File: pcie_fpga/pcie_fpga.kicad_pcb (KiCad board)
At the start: 4 copper layers, 167.7 x 68.9 mm, 26 parts, among them J1 PMOD_Host_Conn_02x06, J2 PCIexpress_x8, J3 PMOD_Host_Conn_02x06, J4 PMOD_Host_Conn_02x06, J5 87832-1420, U2 XCAU10P-1FFVB676I, X1 ECS-2520MVQ-1000-BN-TR

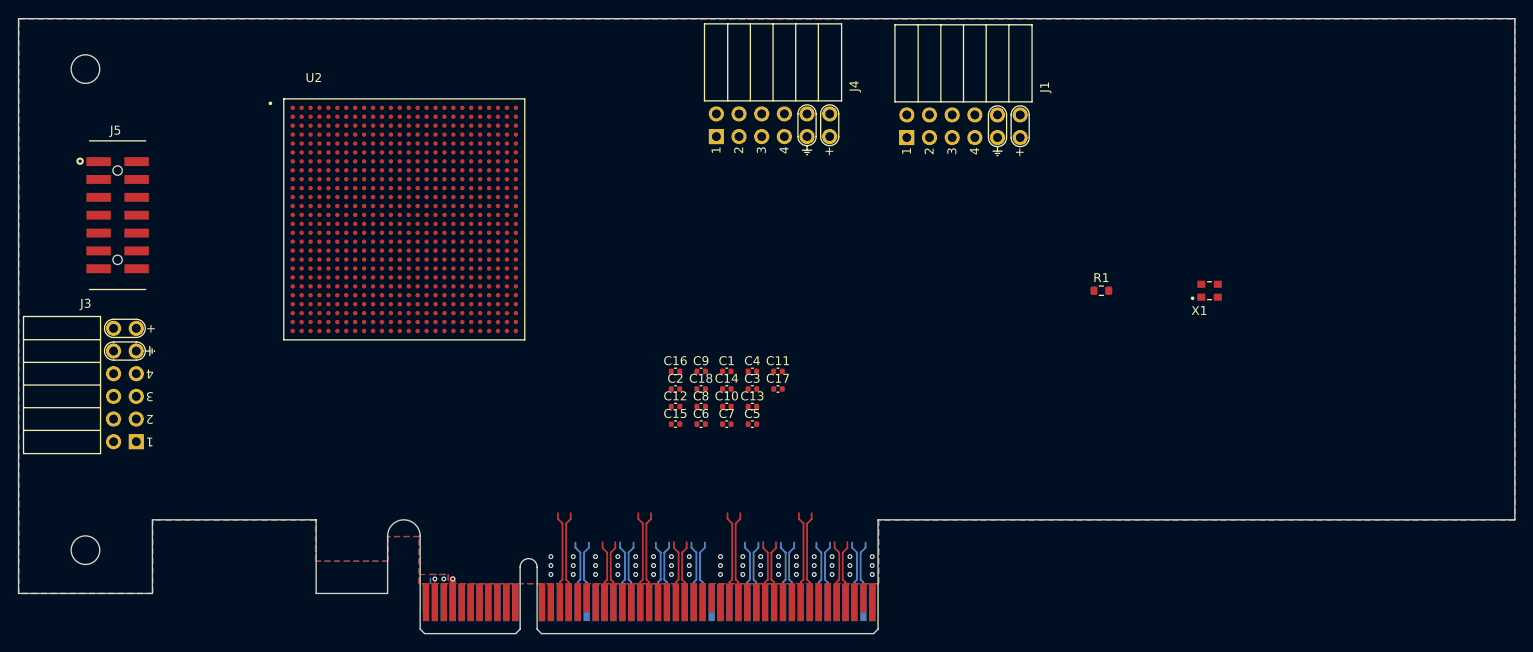
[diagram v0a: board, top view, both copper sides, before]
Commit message: pcie lanes need to be swapped I think.
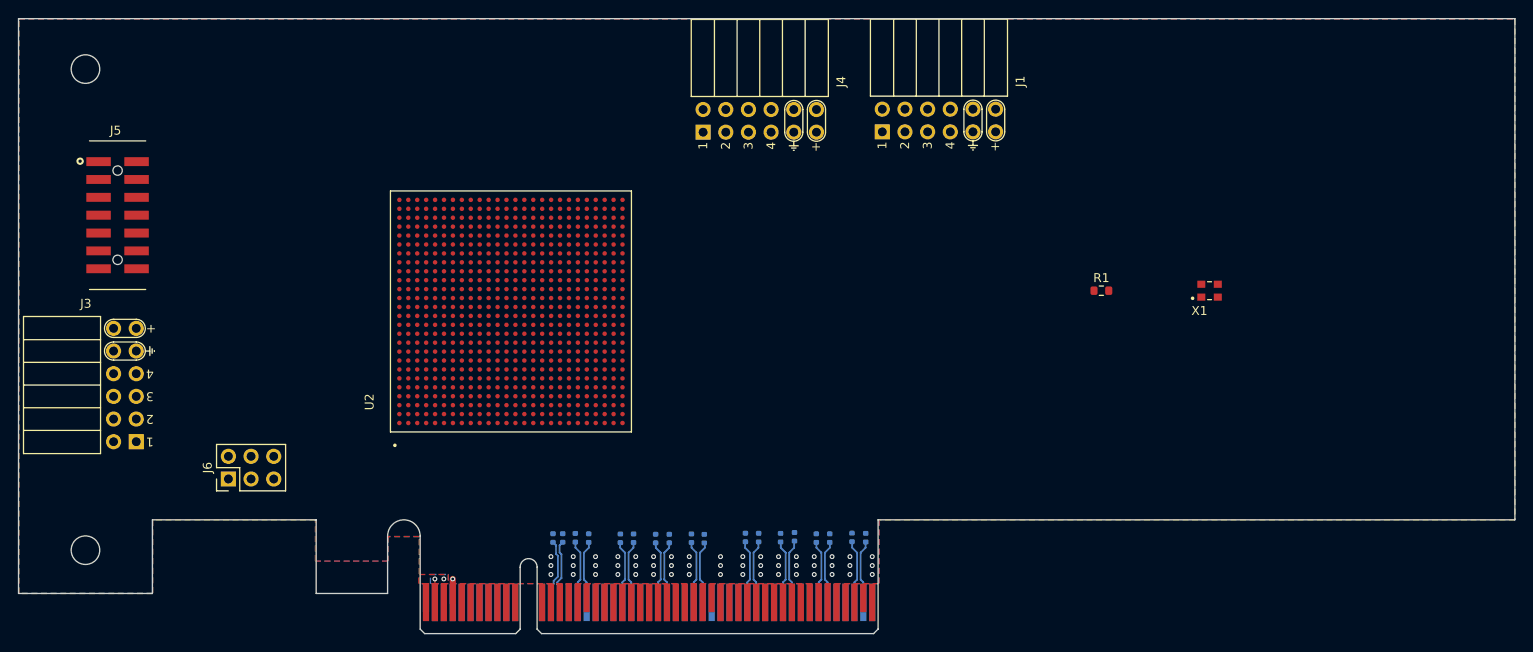
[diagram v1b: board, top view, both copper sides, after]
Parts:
- added J6: Conn_02x03_Odd_Even, Connector_PinHeader_2.54mm:PinHeader_2x03_P2.54mm_Vertical, F.Cu at (88.0, 176.8)
- C1, C10, C11, C12, C13, C14, C15, C16, C17, C18, C2, C3, C4, C5, C6, C7, C8, C9: moved to B.Cu
- moved C3 27.0 mm to (125.4, 183.4), turned to 90 degrees
- moved C4 26.2 mm to (128.4, 183.4), turned to 90 degrees
- moved C16 25.4 mm to (155.4, 183.4), turned to 90 degrees
- moved C1 25.2 mm to (126.9, 183.4), turned to 90 degrees
- moved C18 24.9 mm to (159.4, 183.4), turned to 90 degrees
- moved C2 21.6 mm to (124.4, 183.4), turned to 90 degrees
- moved C15 20.3 mm to (153.9, 183.4), turned to 90 degrees
- moved C5 19.6 mm to (131.9, 183.4), turned to 90 degrees
- moved C11 19.0 mm to (145.9, 183.4), turned to 90 degrees
- moved C9 18.7 mm to (139.9, 183.4), turned to 90 degrees
- moved C17 18.6 mm to (157.9, 183.3), turned to 90 degrees
- moved C14 18.2 mm to (151.4, 183.3), turned to 90 degrees
- moved C12 17.4 mm to (147.4, 183.4), turned to 90 degrees
- moved U2 15.8 mm to (119.6, 158.0), turned to 90 degrees
- moved C8 15.2 mm to (137.4, 183.5), turned to 90 degrees
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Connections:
- J2 pad B17: unconnected-(J2-PadB17) -> /prsnt_x1
- J2 pad B31: unconnected-(J2-PadB31) -> /prsnt_x4
- J2 pad B48: /prsntn -> /prsnt_x8
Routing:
- net /pet6_P: track 10.3 -> 0.00 mm
- net /pet4_P: track 10.3 -> 0.00 mm
- net /pet2_P: track 10.3 -> 0.00 mm
- net /pet6_N: track 10.3 -> 0.00 mm
- net /pet4_N: track 10.3 -> 0.00 mm
- net /pet2_N: track 10.3 -> 0.00 mm
- net /pet0_P: track 10.3 -> 0.00 mm
- net /pet0_N: track 10.3 -> 0.00 mm
- net /refclk_N: track 0.00 -> 7.30 mm
- net /refclk_P: track 0.00 -> 7.28 mm
- net /pet7_P: track 7.09 -> 0.00 mm
- net /pet7_N: track 7.09 -> 0.00 mm
- net /pet5_P: track 7.09 -> 0.00 mm
- net /pet5_N: track 7.09 -> 0.00 mm
- net /pet3_P: track 7.09 -> 0.00 mm
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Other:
- copper layers 4 -> 6

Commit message: swapped the pcie lanes for routing
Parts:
- moved X1 95.6 mm to (102.4, 157.8)
- moved R1 78.5 mm to (107.3, 156.8), turned to 180 degrees
- moved J4 56.2 mm to (85.0, 137.9)
- moved J1 56.2 mm to (105.0, 137.8)
- moved U2 16.7 mm to (136.1, 155.4)
- moved J6 9.11 mm to (84.9, 168.2), turned to 0 degrees
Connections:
- U2 pad AA4: /pre_per4_N -> /pre_per3_N
- U2 pad AA5: /pre_per4_P -> /pre_per3_P
- U2 pad AB1: /pet3_N -> /pet4_N
- U2 pad AB2: /pet3_P -> /pet4_P
- U2 pad AC4: /pre_per3_N -> /pre_per4_N
- U2 pad AC5: /pre_per3_P -> /pre_per4_P
- U2 pad AD1: /pet2_N -> /pet5_N
- U2 pad AD2: /pet2_P -> /pet5_P
- U2 pad AD6: /pre_per2_N -> /pre_per5_N
- U2 pad AD7: /pre_per2_P -> /pre_per5_P
- U2 pad AE3: /pet1_N -> /pet6_N
- U2 pad AE4: /pet1_P -> /pet6_P
- U2 pad AE8: /pre_per1_N -> /pre_per6_N
- U2 pad AE9: /pre_per1_P -> /pre_per6_P
- U2 pad AF1: /pet0_N -> /pet7_N
- U2 pad AF2: /pet0_P -> /pet7_P
- U2 pad AF6: /pre_per0_N -> /pre_per7_N
- U2 pad AF7: /pre_per0_P -> /pre_per7_P
- U2 pad P1: /pet7_N -> /pet0_N
- U2 pad P2: /pet7_P -> /pet0_P
- U2 pad R4: /pre_per7_N -> /pre_per0_N
- U2 pad R5: /pre_per7_P -> /pre_per0_P
- U2 pad T1: /pet6_N -> /pet1_N
- U2 pad T2: /pet6_P -> /pet1_P
- U2 pad U4: /pre_per6_N -> /pre_per1_N
- U2 pad U5: /pre_per6_P -> /pre_per1_P
- U2 pad V1: /pet5_N -> /pet2_N
- U2 pad V2: /pet5_P -> /pet2_P
- U2 pad W4: /pre_per5_N -> /pre_per2_N
- U2 pad W5: /pre_per5_P -> /pre_per2_P
- U2 pad Y1: /pet4_N -> /pet3_N
- U2 pad Y2: /pet4_P -> /pet3_P
